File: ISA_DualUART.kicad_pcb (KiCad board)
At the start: 2 copper layers, 176.5 x 90.2 mm, 74 parts, among them J1 ISA BUS, J10 Parallel Port, J2 ADDR_IRQ, J3 UART1_SEL, J4 UART2_SEL, J6 Serial 2 IDC, J7 Serial 1 DB9, J9 Parport IRQ Select, U1 74LS138, U11 74LS30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

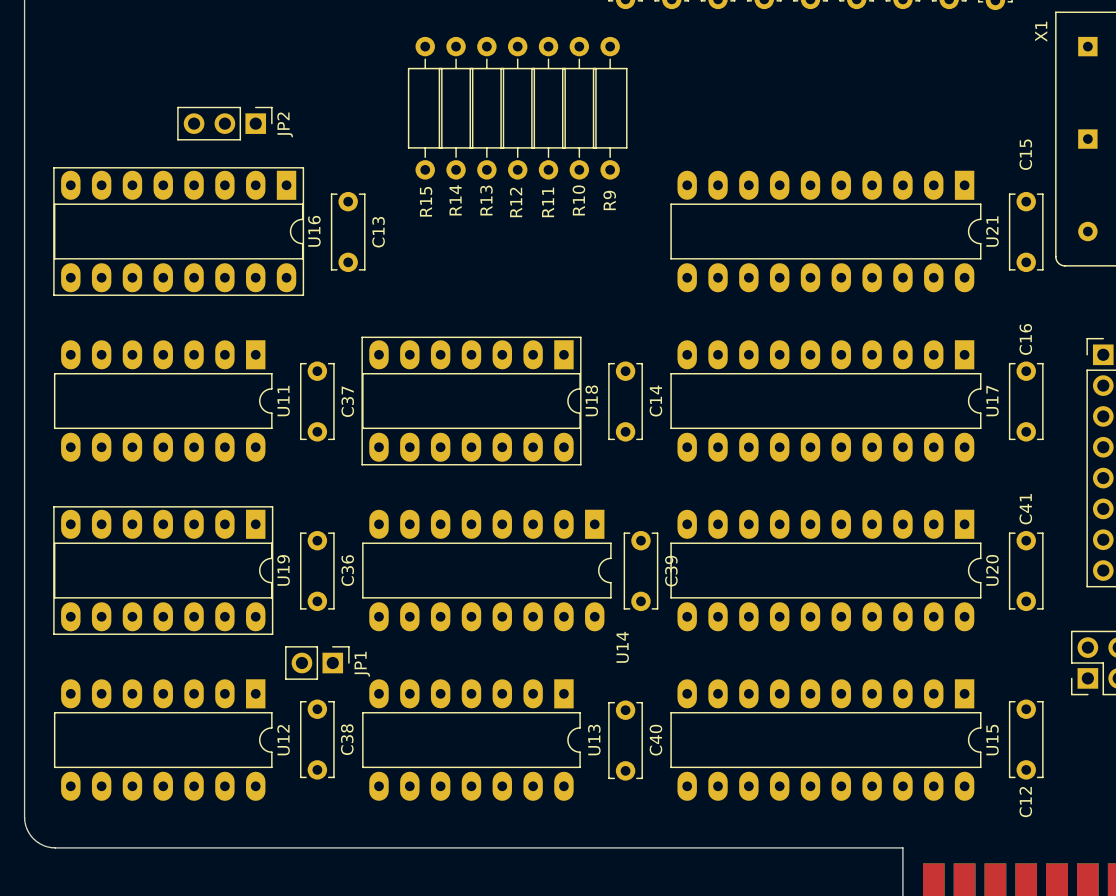
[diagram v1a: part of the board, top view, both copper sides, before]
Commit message: Move some components
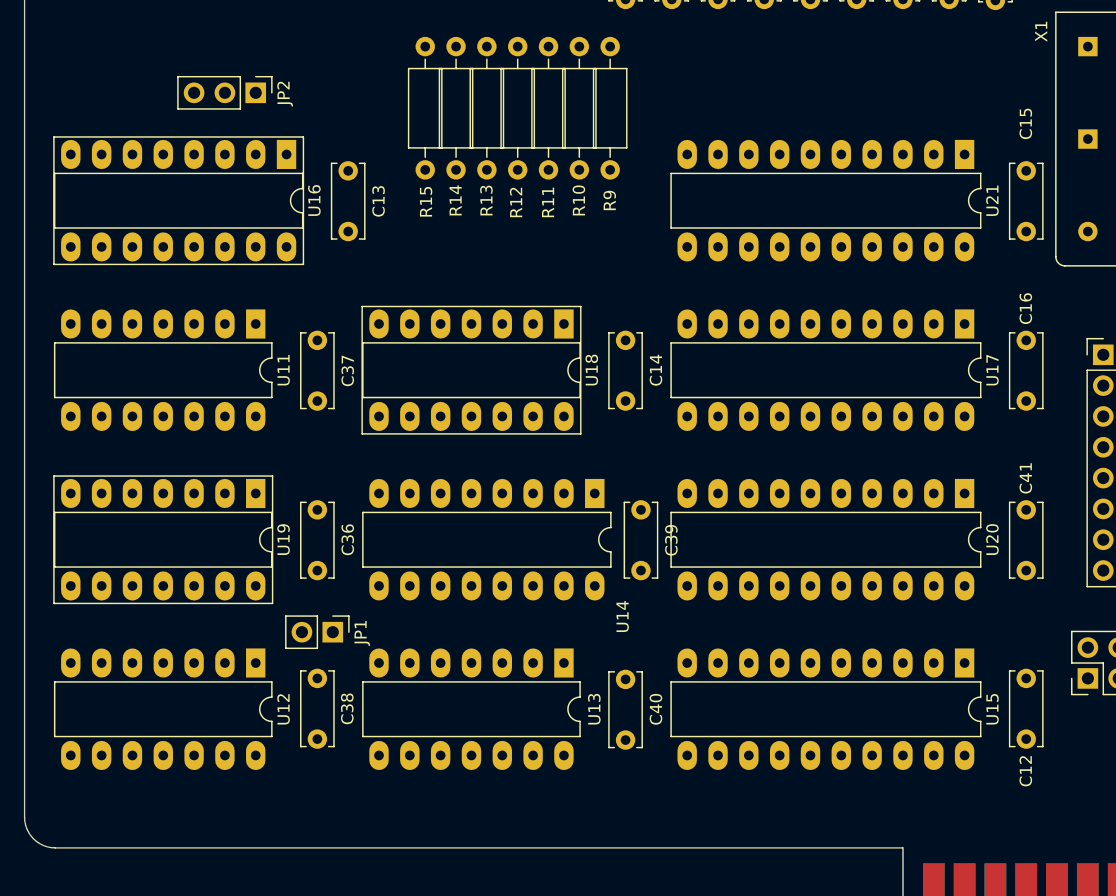
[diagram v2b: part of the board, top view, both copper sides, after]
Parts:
- moved C13 2.54 mm to (165.1, 143.5)
- moved C14 2.54 mm to (188.0, 157.5)
- moved C15 2.54 mm to (221.0, 143.5)
- moved C16 2.54 mm to (221.0, 157.5)
- moved C36 2.54 mm to (162.6, 171.4)
- moved C37 2.54 mm to (162.6, 157.5)
- moved C39 2.54 mm to (189.2, 171.4)
- moved C40 2.54 mm to (188.0, 185.4)
- moved C41 2.54 mm to (221.0, 171.4)
- moved U12 2.54 mm to (157.5, 179.1)
- moved U13 2.54 mm to (182.9, 179.1)
- moved U15 2.54 mm to (215.9, 179.1)
- moved C12 2.54 mm to (221.0, 180.3)
- moved C38 2.54 mm to (162.6, 180.3)
- moved JP1 2.54 mm to (163.8, 176.5)
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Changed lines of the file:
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@@
   )
   (module Capacitor_THT:C_Disc_D6.0mm_W2.5mm_P5.00mm (layer F.Cu)
-    (at 220.98 160.02 90)
+    (at 220.98 157.48 90)
     (descr "C, Disc series, Radial, pin pitch=5.00mm, , diameter*width=6*2.5mm^2, Capacitor, http://cdn-reichelt.de/documents/datenblatt/B300/DS_KERKO_TC.pdf")
     (tags "C Disc series Radial pin pitch 5.00mm  diameter 6mm width 2.5mm Capacitor")
@@
   )
   (module Capacitor_THT:C_Disc_D6.0mm_W2.5mm_P5.00mm (layer F.Cu)
-    (at 220.98 146.05 90)
+    (at 220.98 143.51 90)
     (descr "C, Disc series, Radial, pin pitch=5.00mm, , diameter*width=6*2.5mm^2, Capacitor, http://cdn-reichelt.de/documents/datenblatt/B300/DS_KERKO_TC.pdf")
     (tags "C Disc series Radial pin pitch 5.00mm  diameter 6mm width 2.5mm Capacitor")
@@
   )
   (module Capacitor_THT:C_Disc_D6.0mm_W2.5mm_P5.00mm (layer F.Cu)
-    (at 187.96 160.02 90)
+    (at 187.96 157.48 90)
     (descr "C, Disc series, Radial, pin pitch=5.00mm, , diameter*width=6*2.5mm^2, Capacitor, http://cdn-reichelt.de/documents/datenblatt/B300/DS_KERKO_TC.pdf")
     (tags "C Disc series Radial pin pitch 5.00mm  diameter 6mm width 2.5mm Capacitor")
@@
   )
   (module Capacitor_THT:C_Disc_D6.0mm_W2.5mm_P5.00mm (layer F.Cu)
-    (at 165.1 146.05 90)
+    (at 165.1 143.51 90)
     (descr "C, Disc series, Radial, pin pitch=5.00mm, , diameter*width=6*2.5mm^2, Capacitor, http://cdn-reichelt.de/documents/datenblatt/B300/DS_KERKO_TC.pdf")
     (tags "C Disc series Radial pin pitch 5.00mm  diameter 6mm width 2.5mm Capacitor")
@@
   )
   (module Package_DIP:DIP-20_W7.62mm_LongPads (layer F.Cu)
-    (at 215.9 153.67 270)
+    (at 215.9 151.13 270)
     (descr "20-lead though-hole mounted DIP package, row spacing 7.62 mm (300 mils), LongPads")
     (tags "THT DIP DIL PDIP 2.54mm 7.62mm 300mil LongPads")
@@
   )
   (module Capacitor_THT:C_Disc_D6.0mm_W2.5mm_P5.00mm (layer F.Cu)
-    (at 220.98 173.99 90)
+    (at 220.98 171.45 90)
     (descr "C, Disc series, Radial, pin pitch=5.00mm, , diameter*width=6*2.5mm^2, Capacitor, http://cdn-reichelt.de/documents/datenblatt/B300/DS_KERKO_TC.pdf")
     (tags "C Disc series Radial pin pitch 5.00mm  diameter 6mm width 2.5mm Capacitor")
@@
   )
   (module Capacitor_THT:C_Disc_D6.0mm_W2.5mm_P5.00mm (layer F.Cu)
-    (at 187.96 187.96 90)
+    (at 187.96 185.42 90)
     (descr "C, Disc series, Radial, pin pitch=5.00mm, , diameter*width=6*2.5mm^2, Capacitor, http://cdn-reichelt.de/documents/datenblatt/B300/DS_KERKO_TC.pdf")
     (tags "C Disc series Radial pin pitch 5.00mm  diameter 6mm width 2.5mm Capacitor")
@@
   )
   (module Capacitor_THT:C_Disc_D6.0mm_W2.5mm_P5.00mm (layer F.Cu)
-    (at 189.23 173.99 90)
+    (at 189.23 171.45 90)
     (descr "C, Disc series, Radial, pin pitch=5.00mm, , diameter*width=6*2.5mm^2, Capacitor, http://cdn-reichelt.de/documents/datenblatt/B300/DS_KERKO_TC.pdf")
     (tags "C Disc series Radial pin pitch 5.00mm  diameter 6mm width 2.5mm Capacitor")
@@
   )
   (module Capacitor_THT:C_Disc_D6.0mm_W2.5mm_P5.00mm (layer F.Cu)
-    (at 162.56 182.88 270)
+    (at 162.56 180.34 270)
     (descr "C, Disc series, Radial, pin pitch=5.00mm, , diameter*width=6*2.5mm^2, Capacitor, http://cdn-reichelt.de/documents/datenblatt/B300/DS_KERKO_TC.pdf")
     (tags "C Disc series Radial pin pitch 5.00mm  diameter 6mm width 2.5mm Capacitor")
@@
   )
   (module Capacitor_THT:C_Disc_D6.0mm_W2.5mm_P5.00mm (layer F.Cu)
-    (at 162.56 160.02 90)
+    (at 162.56 157.48 90)
     (descr "C, Disc series, Radial, pin pitch=5.00mm, , diameter*width=6*2.5mm^2, Capacitor, http://cdn-reichelt.de/documents/datenblatt/B300/DS_KERKO_TC.pdf")
     (tags "C Disc series Radial pin pitch 5.00mm  diameter 6mm width 2.5mm Capacitor")
@@
   )
   (module Capacitor_THT:C_Disc_D6.0mm_W2.5mm_P5.00mm (layer F.Cu)
-    (at 162.56 173.99 90)
+    (at 162.56 171.45 90)
     (descr "C, Disc series, Radial, pin pitch=5.00mm, , diameter*width=6*2.5mm^2, Capacitor, http://cdn-reichelt.de/documents/datenblatt/B300/DS_KERKO_TC.pdf")
     (tags "C Disc series Radial pin pitch 5.00mm  diameter 6mm width 2.5mm Capacitor")
@@
   )
   (module Package_DIP:DIP-20_W7.62mm_LongPads (layer F.Cu)
-    (at 215.9 139.7 270)
+    (at 215.9 137.16 270)
     (descr "20-lead though-hole mounted DIP package, row spacing 7.62 mm (300 mils), LongPads")
     (tags "THT DIP DIL PDIP 2.54mm 7.62mm 300mil LongPads")
@@
   )
   (module Package_DIP:DIP-20_W7.62mm_LongPads (layer F.Cu)
-    (at 215.9 167.64 270)
+    (at 215.9 165.1 270)
     (descr "20-lead though-hole mounted DIP package, row spacing 7.62 mm (300 mils), LongPads")
     (tags "THT DIP DIL PDIP 2.54mm 7.62mm 300mil LongPads")
@@
   )
   (module Package_DIP:DIP-14_W7.62mm_Socket_LongPads (layer F.Cu)
-    (at 157.48 167.64 270)
+    (at 157.48 165.1 270)
     (descr "14-lead though-hole mounted DIP package, row spacing 7.62 mm (300 mils), Socket, LongPads")
     (tags "THT DIP DIL PDIP 2.54mm 7.62mm 300mil Socket LongPads")
@@
   )
   (module Package_DIP:DIP-14_W7.62mm_Socket_LongPads (layer F.Cu)
-    (at 182.88 153.67 270)
+    (at 182.88 151.13 270)
     (descr "14-lead though-hole mounted DIP package, row spacing 7.62 mm (300 mils), Socket, LongPads")
     (tags "THT DIP DIL PDIP 2.54mm 7.62mm 300mil Socket LongPads")
@@
   )
   (module Package_DIP:DIP-16_W7.62mm_Socket_LongPads (layer F.Cu)
-    (at 160.02 139.7 270)
+    (at 160.02 137.16 270)
     (descr "16-lead though-hole mounted DIP package, row spacing 7.62 mm (300 mils), Socket, LongPads")
     (tags "THT DIP DIL PDIP 2.54mm 7.62mm 300mil Socket LongPads")
@@
   )
   (module Package_DIP:DIP-20_W7.62mm_LongPads (layer F.Cu)
-    (at 215.9 181.61 270)
+    (at 215.9 179.07 270)
     (descr "20-lead though-hole mounted DIP package, row spacing 7.62 mm (300 mils), LongPads")
     (tags "THT DIP DIL PDIP 2.54mm 7.62mm 300mil LongPads")
@@
   )
   (module Package_DIP:DIP-16_W7.62mm_LongPads (layer F.Cu)
-    (at 185.42 167.64 270)
+    (at 185.42 165.1 270)
     (descr "16-lead though-hole mounted DIP package, row spacing 7.62 mm (300 mils), LongPads")
     (tags "THT DIP DIL PDIP 2.54mm 7.62mm 300mil LongPads")
@@
   )
   (module Package_DIP:DIP-14_W7.62mm_LongPads (layer F.Cu)
-    (at 182.88 181.61 270)
+    (at 182.88 179.07 270)
     (descr "14-lead though-hole mounted DIP package, row spacing 7.62 mm (300 mils), LongPads")
     (tags "THT DIP DIL PDIP 2.54mm 7.62mm 300mil LongPads")
@@
   )
   (module Package_DIP:DIP-14_W7.62mm_LongPads (layer F.Cu)
-    (at 157.48 181.61 270)
+    (at 157.48 179.07 270)
     (descr "14-lead though-hole mounted DIP package, row spacing 7.62 mm (300 mils), LongPads")
     (tags "THT DIP DIL PDIP 2.54mm 7.62mm 300mil LongPads")
@@
   )
   (module Package_DIP:DIP-14_W7.62mm_LongPads (layer F.Cu)
-    (at 157.48 153.67 270)
+    (at 157.48 151.13 270)
     (descr "14-lead though-hole mounted DIP package, row spacing 7.62 mm (300 mils), LongPads")
     (tags "THT DIP DIL PDIP 2.54mm 7.62mm 300mil LongPads")
@@
   )
   (module Connector_PinHeader_2.54mm:PinHeader_1x03_P2.54mm_Vertical (layer F.Cu)
-    (at 157.48 134.62 270)
+    (at 157.48 132.08 270)
     (descr "Through hole straight pin header, 1x03, 2.54mm pitch, single row")
     (tags "Through hole pin header THT 1x03 2.54mm single row")
@@
   )
   (module Connector_PinHeader_2.54mm:PinHeader_1x02_P2.54mm_Vertical (layer F.Cu)
-    (at 163.83 179.07 270)
+    (at 163.83 176.53 270)
     (descr "Through hole straight pin header, 1x02, 2.54mm pitch, single row")
     (tags "Through hole pin header THT 1x02 2.54mm single row")
@@
   )
   (module Capacitor_THT:C_Disc_D6.0mm_W2.5mm_P5.00mm (layer F.Cu)
-    (at 220.98 182.88 270)
+    (at 220.98 180.34 270)
     (descr "C, Disc series, Radial, pin pitch=5.00mm, , diameter*width=6*2.5mm^2, Capacitor, http://cdn-reichelt.de/documents/datenblatt/B300/DS_KERKO_TC.pdf")
     (tags "C Disc series Radial pin pitch 5.00mm  diameter 6mm width 2.5mm Capacitor")

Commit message: Chane connector
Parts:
- J10: footprint Connector_PinSocket_2.54mm:PinSocket_2x13_P2.54mm_Vertical -> Connector_PinHeader_2.54mm:PinHeader_2x13_P2.54mm_Vertical
- moved J10 2.54 mm to (177.8, 118.1)
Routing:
- added copper zone on B.Cu, net GND
- added copper zone on F.Cu, net GND

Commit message: Update PCB
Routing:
- net GND: track 0.00 -> 809.3 mm, vias 0 -> 14
- net VCC: track 0.00 -> 765.0 mm, vias 0 -> 7
- net /A6: track 0.00 -> 336.5 mm, vias 0 -> 1
- net /~IOW: track 0.00 -> 216.0 mm, vias 0 -> 3
- net /RESETDRV: track 0.00 -> 212.8 mm, vias 0 -> 7
- net /A0: track 0.00 -> 197.7 mm, vias 0 -> 2
- net /~IOR: track 0.00 -> 183.6 mm, vias 0 -> 2
- net /D7: track 0.00 -> 183.0 mm, vias 0 -> 4
- net /A1: track 0.00 -> 182.5 mm, vias 0 -> 2
- net +12V: track 0.00 -> 175.5 mm, vias 0 -> 2
- net /A3: track 0.00 -> 175.3 mm, vias 0 -> 3
- net /D6: track 0.00 -> 173.5 mm, vias 0 -> 2
- net /A4: track 0.00 -> 172.3 mm, vias 0 -> 2
- net -12V: track 0.00 -> 172.3 mm, vias 0 -> 1
- net /A5: track 0.00 -> 170.0 mm, vias 0 -> 3
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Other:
- board text added: "1-2 -> Bidirectional 2-3 -> Standard"
- board text added: "1.8432Mhz"
- board text added: "16C550"
- board text added: "2E8"
- board text added: "2F8"
- board text added: "3E8"
- board text added: "3F8"
- board text added: "74LS02"
- board text added: "74LS05"
- board text added: "74LS125"
- board text added: "74LS138"
- board text added: "74LS155"
- board text added: "74LS174"
- board text added: "74LS240"
- board text added: "74LS244"
- board text added: "74LS245"
- board text added: "74LS30"
- board text added: "74LS374"
- board text added: "74LS86"
- board text added: "75232"
- board text added: "Closed -> 0x278 Open -> 0x378"
- board text added: "IRQ3"
- board text added: "IRQ4"
- board text added: "IRQ5"
- board text added: "IRQ7"
- board text added: "PP IRQ"
- board text added: "Parallel Port"
- board text added: "RX1"
- board text added: "RX2"
- board text added: "SER1"
- board text added: "SER2"
- board text added: "Serial port 1"
- board text added: "Serial port 2"
- board text added: "TX1"
- board text added: "TX2"
